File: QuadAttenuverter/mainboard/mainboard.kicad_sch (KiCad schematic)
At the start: 65 parts, among them U1 LM324, U2 LM324, U3 LM324, U4 LM324, U5 LM324

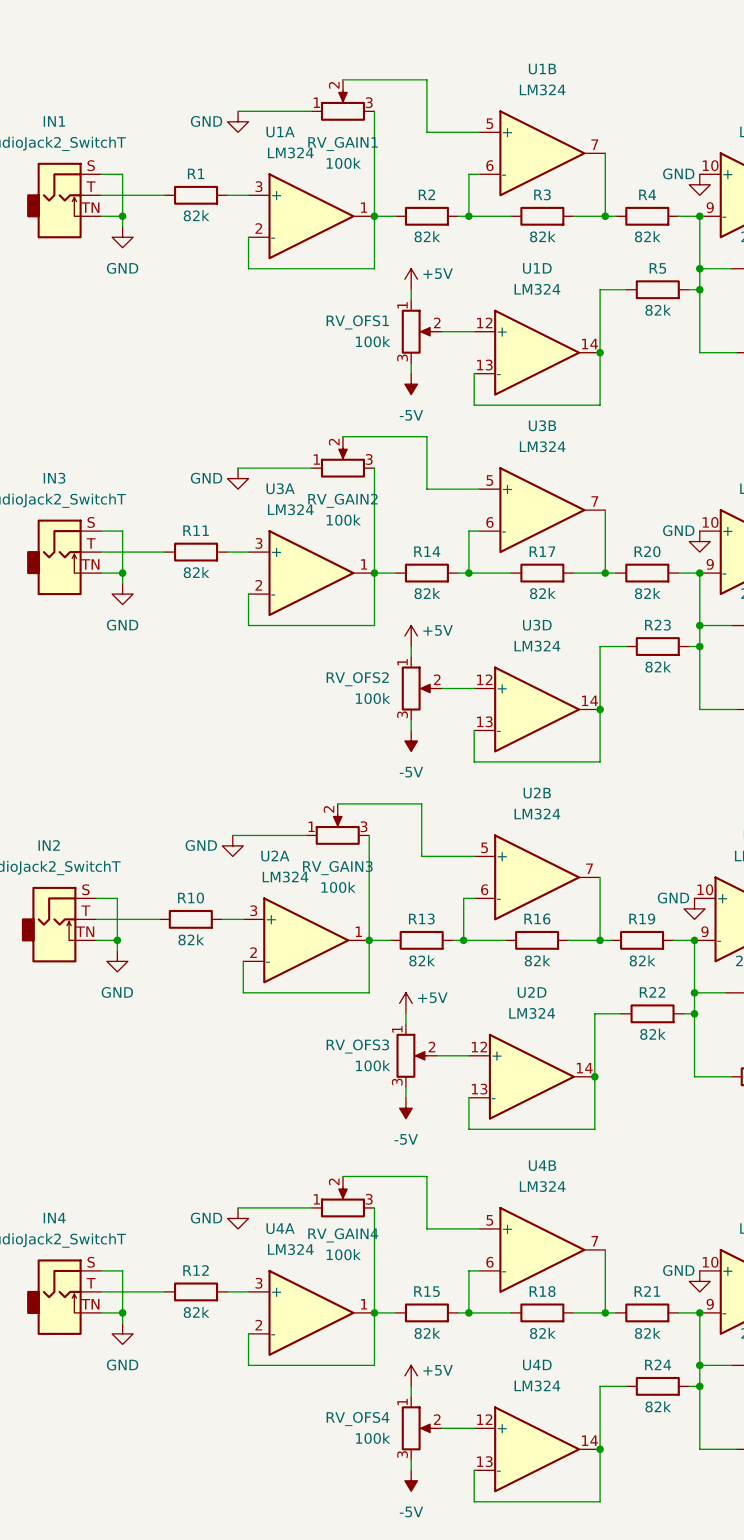
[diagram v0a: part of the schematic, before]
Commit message: Add resistors to make pots more center sensitive
Idea from here:
https://kassu2000.blogspot.com/2018/04/precision-attenuverter-mixer.html
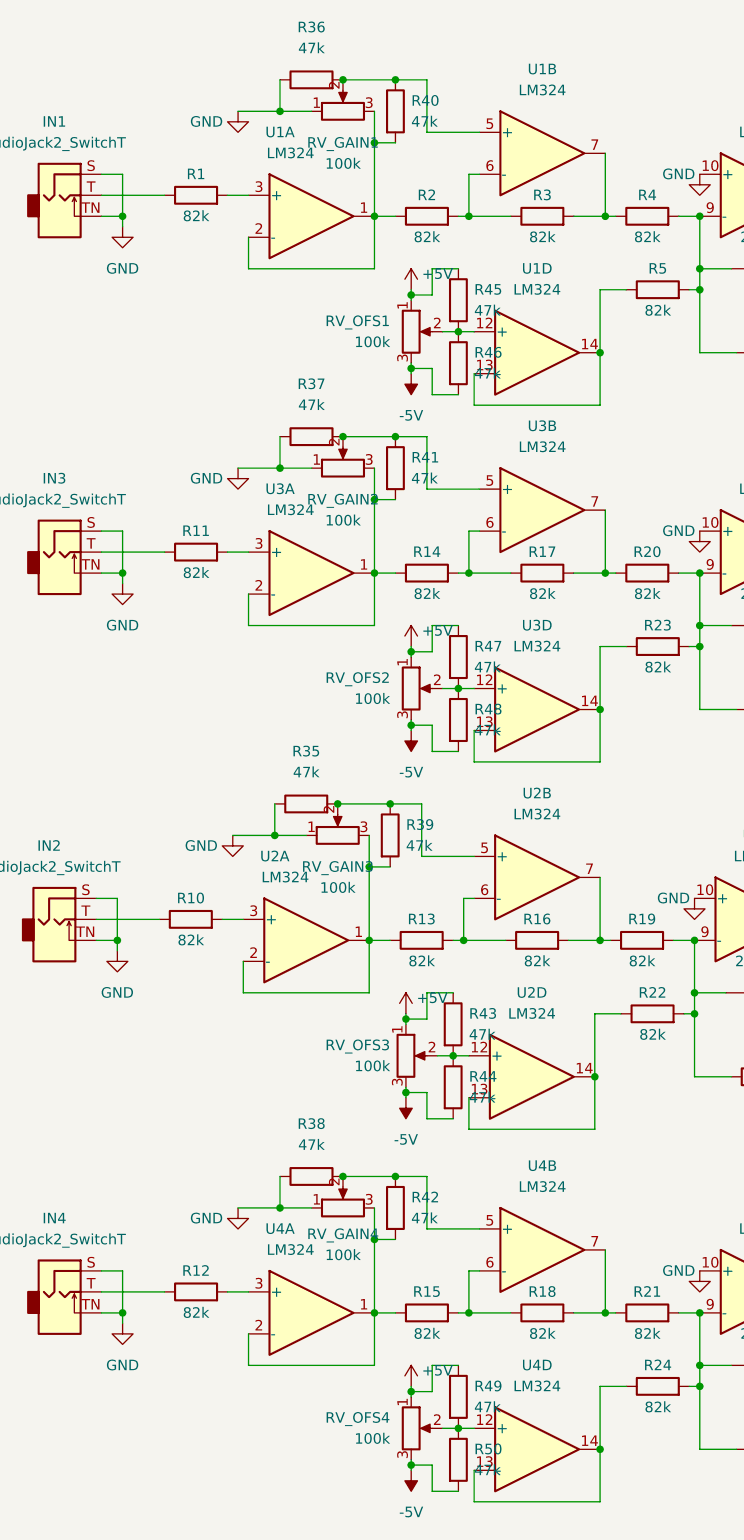
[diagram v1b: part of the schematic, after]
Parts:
- added R35, R36, R37, R38, R39, R40, R41, R42, R43, R44, R45, R46, R47, R48, R49, R50: 47k, Resistor_SMD:R_0603_1608Metric_Pad0.98x0.95mm_HandSolder, symbol Device:R
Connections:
- net +5V: now also R43.1, R45.1, R47.1, R49.1
- net -5V: now also R44.2, R46.2, R48.2, R50.2
- net GND: now also R35.1, R36.1, R37.1, R38.1
- net at R14.1, RV_GAIN2.3, U3.1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: now also R41.2
- net at RV_OFS4.2, U4.12 (+): now also R49.2, R50.1
- net at R13.1, RV_GAIN3.3, U2.1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: now also R39.2
- net at RV_GAIN2.2, U3.5 (+): now also R37.2, R41.1
- net at R15.1, RV_GAIN4.3, U4.1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: now also R42.2
- net at RV_GAIN1.2, U1.5 (+): now also R36.2, R40.1
- net at R2.1, RV_GAIN1.3, U1.1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: now also R40.2
- net at RV_OFS2.2, U3.12 (+): now also R47.2, R48.1
- net at RV_GAIN3.2, U2.5 (+): now also R35.2, R39.1
- net at RV_OFS3.2, U2.12 (+): now also R43.2, R44.1
- net at RV_GAIN4.2, U4.5 (+): now also R38.2, R42.1
- net at RV_OFS1.2, U1.12 (+): now also R45.2, R46.1

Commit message: Final preparations for board splitup
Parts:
- added J1: Conn_01x09, Connector_PinHeader_2.54mm:PinHeader_1x09_P2.54mm_Vertical, symbol Connector_Generic:Conn_01x09
- added J2: Conn_02x10_Counter_Clockwise, Connector_PinHeader_2.54mm:PinHeader_2x10_P2.54mm_Vertical, symbol Connector_Generic:Conn_02x10_Counter_Clockwise
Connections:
- net +5V: now also J2.11 (Pin_11)
- net -5V: now also J2.20 (Pin_20)
- net GND: now also D1.1 (KA), D2.1 (KA), D3.1 (KA), D4.1 (KA), J1.9 (Pin_9), J2.10 (Pin_10); no longer R31.2, R32.2, R33.2, R34.2
- net LED1: now also D1.2 (AK), R31.2, J2.15 (Pin_15)
- net LED2: now also D2.2 (AK), R32.2, J2.14 (Pin_14)
- net LED3: now also D3.2 (AK), R33.2, J2.13 (Pin_13)
- net LED4: now also D4.2 (AK), R34.2, J2.12 (Pin_12)
- net at R33.1: now also U5.8; no longer D3.1 (KA)
- net GAIN2IN: now reaches R14.1, R41.2, RV_GAIN2.3, U3.1, U3.2 (-)
- net GAIN2IN: now also J2.3 (Pin_3)
- net GAIN1OUT: now reaches R36.2, R40.1, RV_GAIN1.2, U1.5 (+)
- net GAIN1OUT: now also J2.2 (Pin_2)
- net OFFSET4: now reaches R49.2, R50.1, RV_OFS4.2, U4.12 (+)
- net OFFSET4: now also J2.16 (Pin_16)
- net OUT1: now reaches OUT1.T, R6.2, R7.2
- net OUT1: now also J1.2 (Pin_2)
- net IN2: now reaches IN3.T, R11.1
- net IN2: now also J1.3 (Pin_3)
- net GAIN3IN: now reaches R13.1, R39.2, RV_GAIN3.3, U2.1, U2.2 (-)
- net GAIN3IN: now also J2.5 (Pin_5)
- net at R32.1: now also U5.7; no longer D2.1 (KA)
- net GAIN2OUT: now reaches R37.2, R41.1, RV_GAIN2.2, U3.5 (+)
- net GAIN2OUT: now also J2.4 (Pin_4)
- net at U5.1: now also R31.1; no longer D1.2 (AK)
- net GAIN4IN: now reaches R15.1, R42.2, RV_GAIN4.3, U4.1, U4.2 (-)
- net GAIN4IN: now also J2.7 (Pin_7)
- net OUT4: now reaches OUT4.T, R27.2, R30.2
- net OUT4: now also J1.8 (Pin_8)
- net OFFSET3: now reaches R43.2, R44.1, RV_OFS3.2, U2.12 (+)
- net OFFSET3: now also J2.17 (Pin_17)
- net GAIN1IN: now reaches R2.1, R40.2, RV_GAIN1.3, U1.1, U1.2 (-)
- net GAIN1IN: now also J2.1 (Pin_1)
- net IN4: now reaches IN4.T, R12.1
- net IN4: now also J1.7 (Pin_7)
- net OFFSET2: now reaches R47.2, R48.1, RV_OFS2.2, U3.12 (+)
- net OFFSET2: now also J2.18 (Pin_18)
- net OUT3: now reaches OUT2.T, R25.2, R28.2
- net OUT3: now also J1.6 (Pin_6)
- net IN1: now reaches IN1.T, R1.1
- net IN1: now also J1.1 (Pin_1)
- net GAIN3OUT: now reaches R35.2, R39.1, RV_GAIN3.2, U2.5 (+)
- net GAIN3OUT: now also J2.6 (Pin_6)
- net at R34.1: now also U5.14; no longer D4.1 (KA)
- net IN3: now reaches IN2.T, R10.1
- net IN3: now also J1.5 (Pin_5)
- net OFFSET1: now reaches R45.2, R46.1, RV_OFS1.2, U1.12 (+)
- net OFFSET1: now also J2.19 (Pin_19)
- net GAIN4OUT: now reaches R38.2, R42.1, RV_GAIN4.2, U4.5 (+)
- net GAIN4OUT: now also J2.8 (Pin_8)
- net OUT2: now reaches OUT3.T, R26.2, R29.2
- net OUT2: now also J1.4 (Pin_4)
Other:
- moved on the sheet: D1, D2, D3, D4, R31, R32, R33, R34

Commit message: Fixed duplicate net names for LEDn
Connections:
- net LED1: no longer 22pF1.2, R7.1, U1.8, U5.3 (+)
- net LED2: no longer 22pF3.2, R29.1, U3.8, U5.5 (+)
- net LED3: no longer 22pF2.2, R28.1, U2.8, U5.10 (+)
- net LED4: no longer 22pF4.2, R30.1, U4.8, U5.12 (+)
- new net LEDSIG1: 22pF1.2, R7.1, U1.8, U5.3 (+)
- new net LEDSIG2: 22pF3.2, R29.1, U3.8, U5.5 (+)
- new net LEDSIG3: 22pF2.2, R28.1, U2.8, U5.10 (+)
- new net LEDSIG4: 22pF4.2, R30.1, U4.8, U5.12 (+)
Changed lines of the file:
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@@
     (effects (font (size 1.27 1.27)) (justify left bottom))
   )
-  (label "LED3" (at 202.565 114.3 180)
+  (label "LEDSIG3" (at 202.565 114.3 180)
     (effects (font (size 1.27 1.27)) (justify right bottom))
   )
@@
     (effects (font (size 1.27 1.27)) (justify right bottom))
   )
-  (label "LED2" (at 202.565 102.87 180)
+  (label "LEDSIG2" (at 202.565 102.87 180)
     (effects (font (size 1.27 1.27)) (justify right bottom))
   )
@@
     (effects (font (size 1.27 1.27)) (justify left bottom))
   )
-  (label "LED1" (at 130.175 38.1 0)
+  (label "LEDSIG1" (at 130.175 38.1 0)
     (effects (font (size 1.27 1.27)) (justify left bottom))
   )
-  (label "LED2" (at 130.175 81.28 0)
+  (label "LEDSIG2" (at 130.175 81.28 0)
     (effects (font (size 1.27 1.27)) (justify left bottom))
   )
@@
     (effects (font (size 1.27 1.27)) (justify left bottom))
   )
-  (label "LED4" (at 202.565 125.73 180)
+  (label "LEDSIG4" (at 202.565 125.73 180)
     (effects (font (size 1.27 1.27)) (justify right bottom))
   )
-  (label "LED4" (at 130.175 170.815 0)
+  (label "LEDSIG4" (at 130.175 170.815 0)
     (effects (font (size 1.27 1.27)) (justify left bottom))
   )
@@
     (effects (font (size 1.27 1.27)) (justify left bottom))
   )
-  (label "LED3" (at 129.54 125.73 0)
+  (label "LEDSIG3" (at 129.54 125.73 0)
     (effects (font (size 1.27 1.27)) (justify left bottom))
   )
@@
     (effects (font (size 1.27 1.27)) (justify right bottom))
   )
-  (label "LED1" (at 202.565 91.44 180)
+  (label "LEDSIG1" (at 202.565 91.44 180)
     (effects (font (size 1.27 1.27)) (justify right bottom))
   )

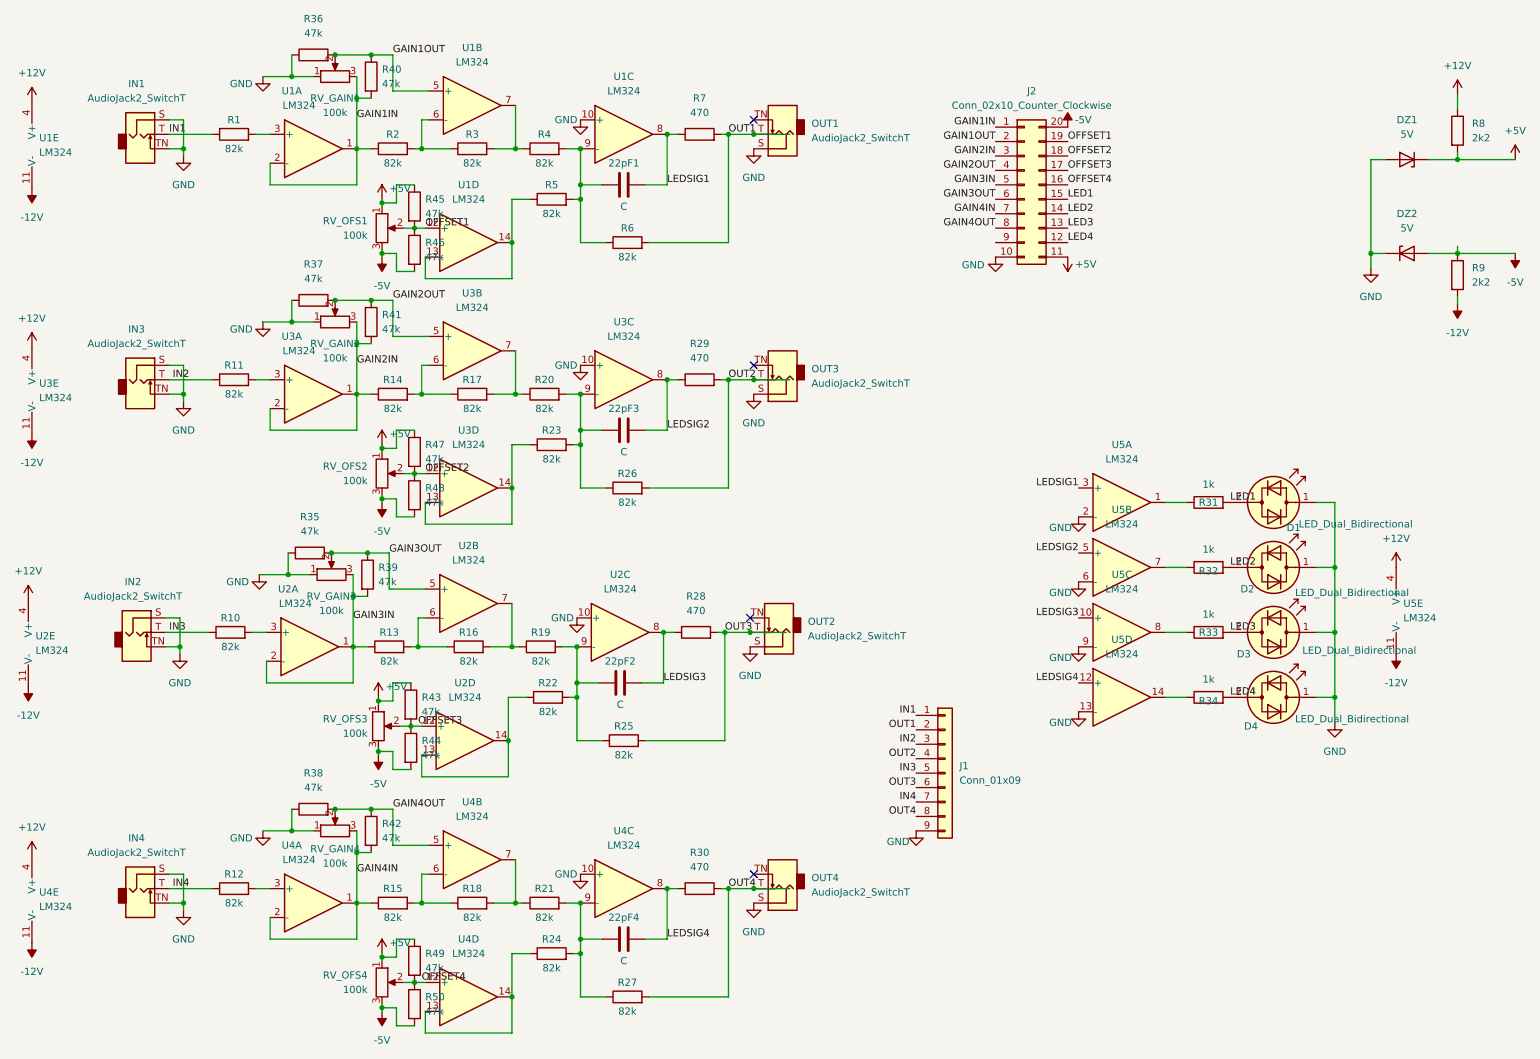
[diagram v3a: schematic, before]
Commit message: Initial routing of ioboard
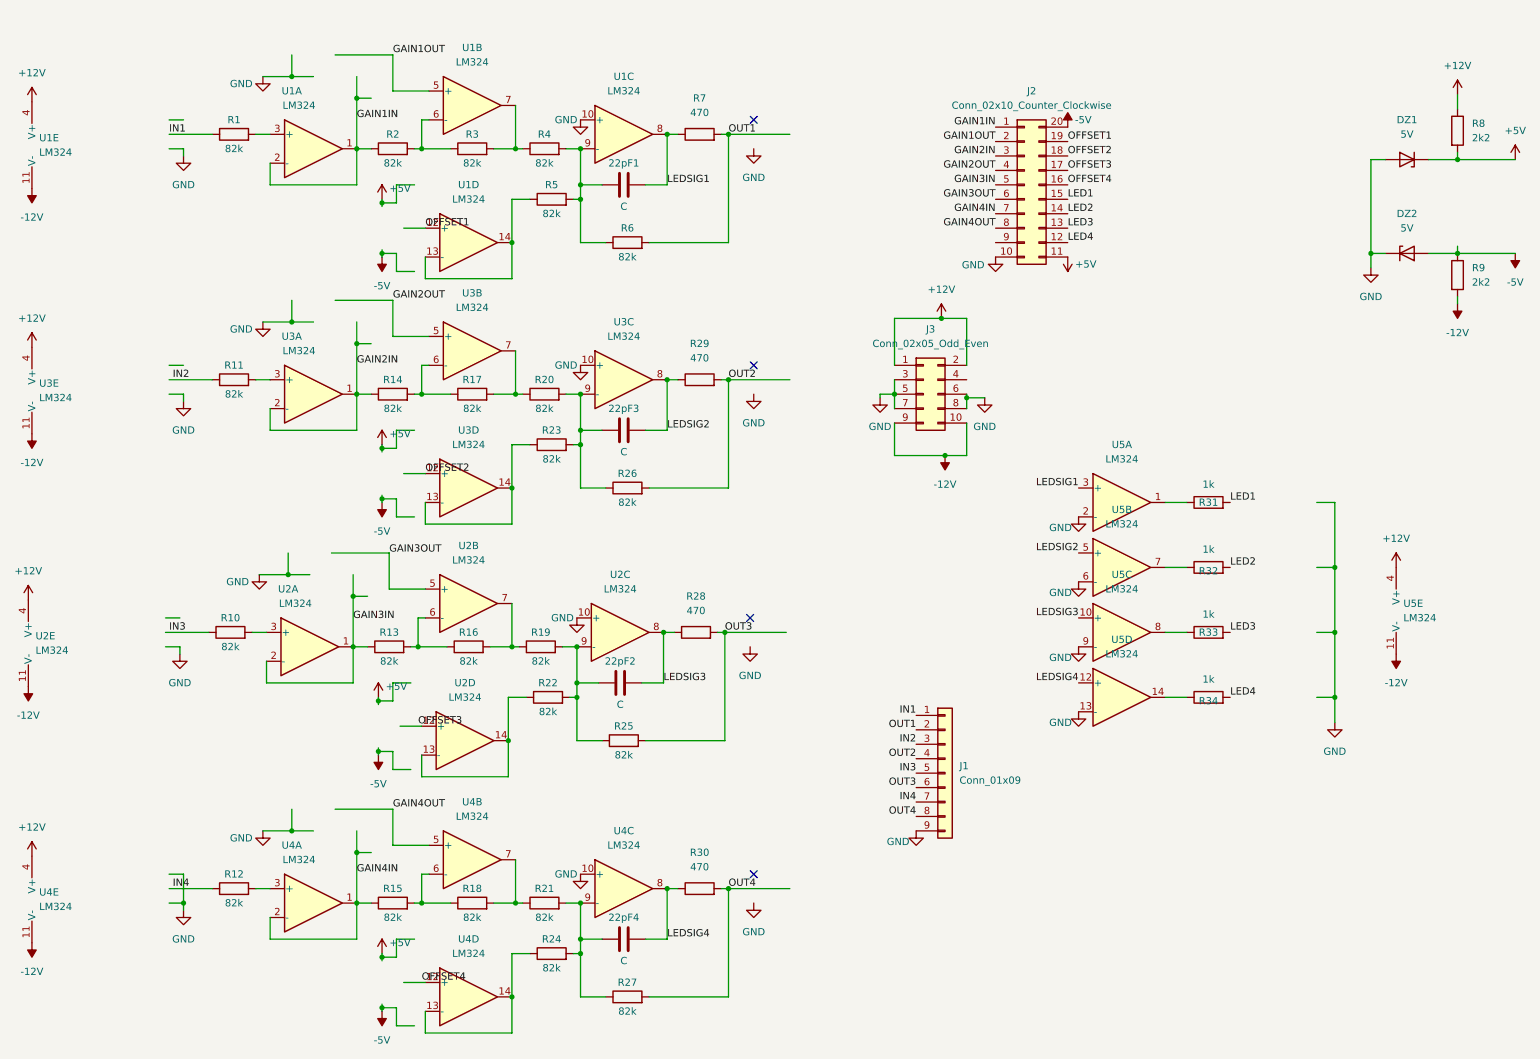
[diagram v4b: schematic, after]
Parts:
- removed D1, D2, D3, D4: LED_Dual_Bidirectional, LED_THT:LED_D3.0mm, symbol Device:LED_Dual_Bidirectional
- removed IN1, IN2, IN3, IN4, OUT1, OUT2, OUT3, OUT4: AudioJack2_SwitchT, Connector_Audio:Jack_3.5mm_QingPu_WQP-PJ398SM_Vertical_CircularHoles, symbol Connector:AudioJack2_SwitchT
- removed R35, R36, R37, R38, R39, R40, R41, R42, R43, R44, R45, R46, R47, R48, R49, R50: 47k, Resistor_SMD:R_0603_1608Metric_Pad0.98x0.95mm_HandSolder, symbol Device:R
- removed RV_GAIN1, RV_GAIN2, RV_GAIN3, RV_GAIN4, RV_OFS1, RV_OFS2, RV_OFS3, RV_OFS4: 100k, Potentiometer_THT:Potentiometer_Alps_RK09K_Single_Vertical, symbol Device:R_Potentiometer
- added J3: Conn_02x05_Odd_Even, Connector_PinHeader_2.54mm:PinHeader_2x05_P2.54mm_Vertical, symbol Connector_Generic:Conn_02x05_Odd_Even
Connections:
- net +12V: now also J3.1 (Pin_1), J3.2 (Pin_2)
- net -12V: now also J3.10 (Pin_10), J3.9 (Pin_9)
- net GND: now also J3.3 (Pin_3), J3.5 (Pin_5), J3.6 (Pin_6), J3.7 (Pin_7), J3.8 (Pin_8)

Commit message: Add IOBoard with the right knob distance
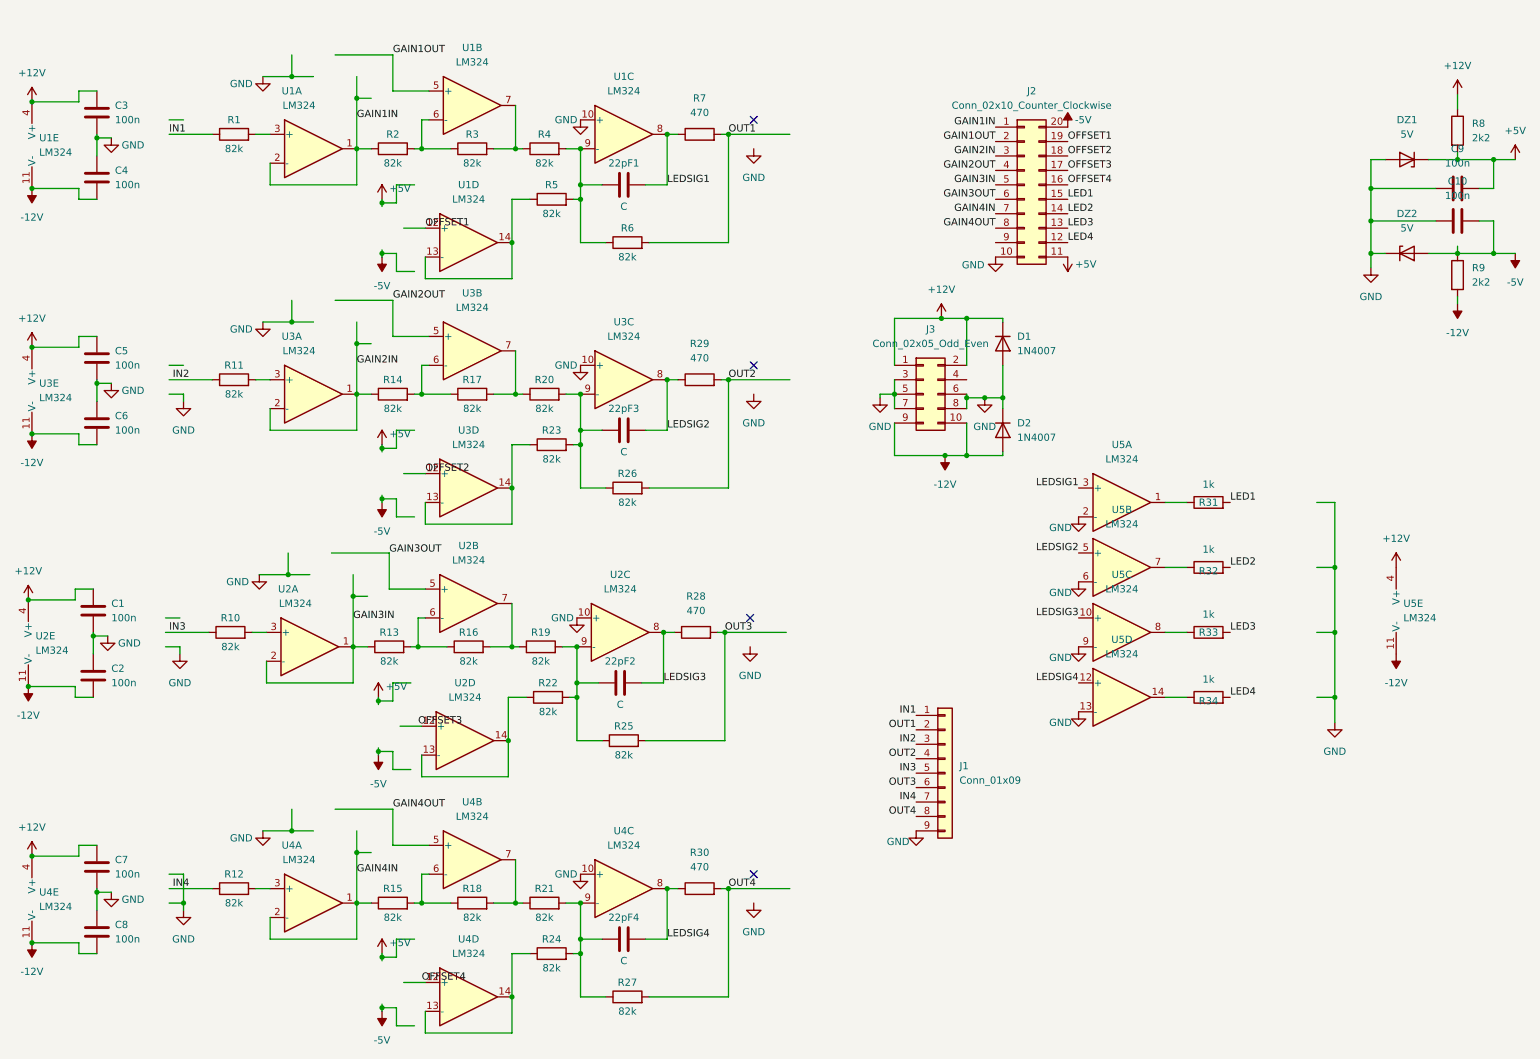
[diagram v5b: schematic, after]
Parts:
- added C1, C10, C2, C3, C4, C5, C6, C7, C8, C9: 100n, Capacitor_SMD:C_0603_1608Metric_Pad1.08x0.95mm_HandSolder, symbol Device:C
- added D1, D2: 1N4007, Diode_THT:D_DO-41_SOD81_P7.62mm_Horizontal, symbol Device:D
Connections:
- net +12V: now also C1.1, C3.1, C5.1, C7.1, D1.1 (K)
- net +5V: now also C9.2
- net -12V: now also C2.2, C4.2, C6.2, C8.2, D2.2 (A)
- net -5V: now also C10.2
- net GND: now also C1.2, C10.1, C2.1, C3.2, C4.1, C5.2, C6.1, C7.2, C8.1, C9.1, D1.2 (A), D2.1 (K)
